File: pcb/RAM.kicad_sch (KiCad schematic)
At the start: 3 parts, among them U63 APS6404L-3SQRx-SN

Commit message: Cleaning
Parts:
- C63: Manufacturer_Part_Number (none) -> GRM188R71H104KA93D
- FB31: Manufacturer_Part_Number (none) -> WLBD1608HCU101TL
- U63: Manufacturer_Part_Number (none) -> APS6404L-3SQR

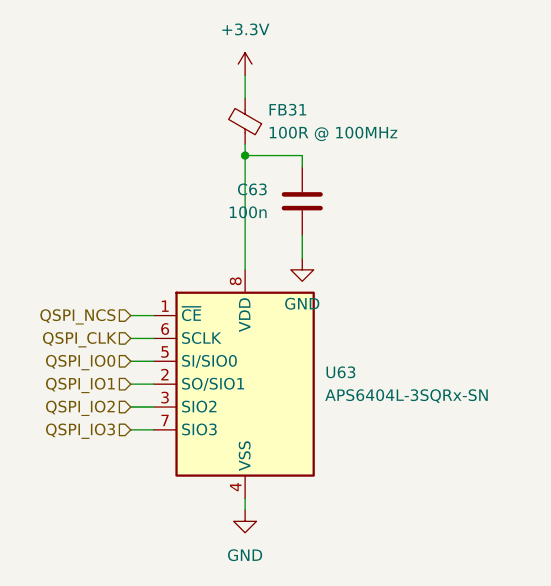
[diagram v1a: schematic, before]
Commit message: Fix BOM data: 1k resistor MPN, 1N4148WS diodes, ADuM/DAC7311 orderable part numbers, BOM export settings
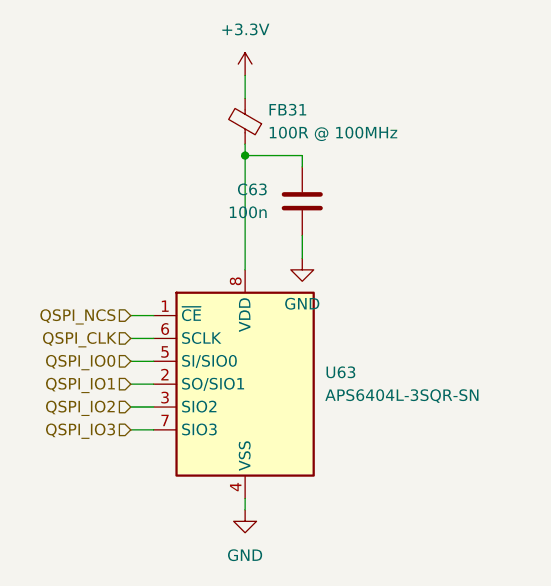
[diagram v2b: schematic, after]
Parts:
- U63: value APS6404L-3SQRx-SN -> APS6404L-3SQR-SN
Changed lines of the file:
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@@
 			)
 		)
-		(property "Description" "WLBD1608HCU101TL"
+		(property "Description" ""
 			(at 119.38 67.31 0)
 			(hide yes)
@@
 			)
 		)
-		(property "Value" "APS6404L-3SQRx-SN"
+		(property "Value" "APS6404L-3SQR-SN"
 			(at 128.27 97.7899 0)
 			(show_name no)
